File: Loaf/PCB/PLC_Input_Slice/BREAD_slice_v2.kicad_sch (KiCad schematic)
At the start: 12 parts, among them J1 10018783-10200TLF, J2 Conn_01x01_Socket, J3 Conn_01x01_Socket, J4 Conn_01x01_Socket, J5 Conn_01x01_Socket, U2 MCP3208

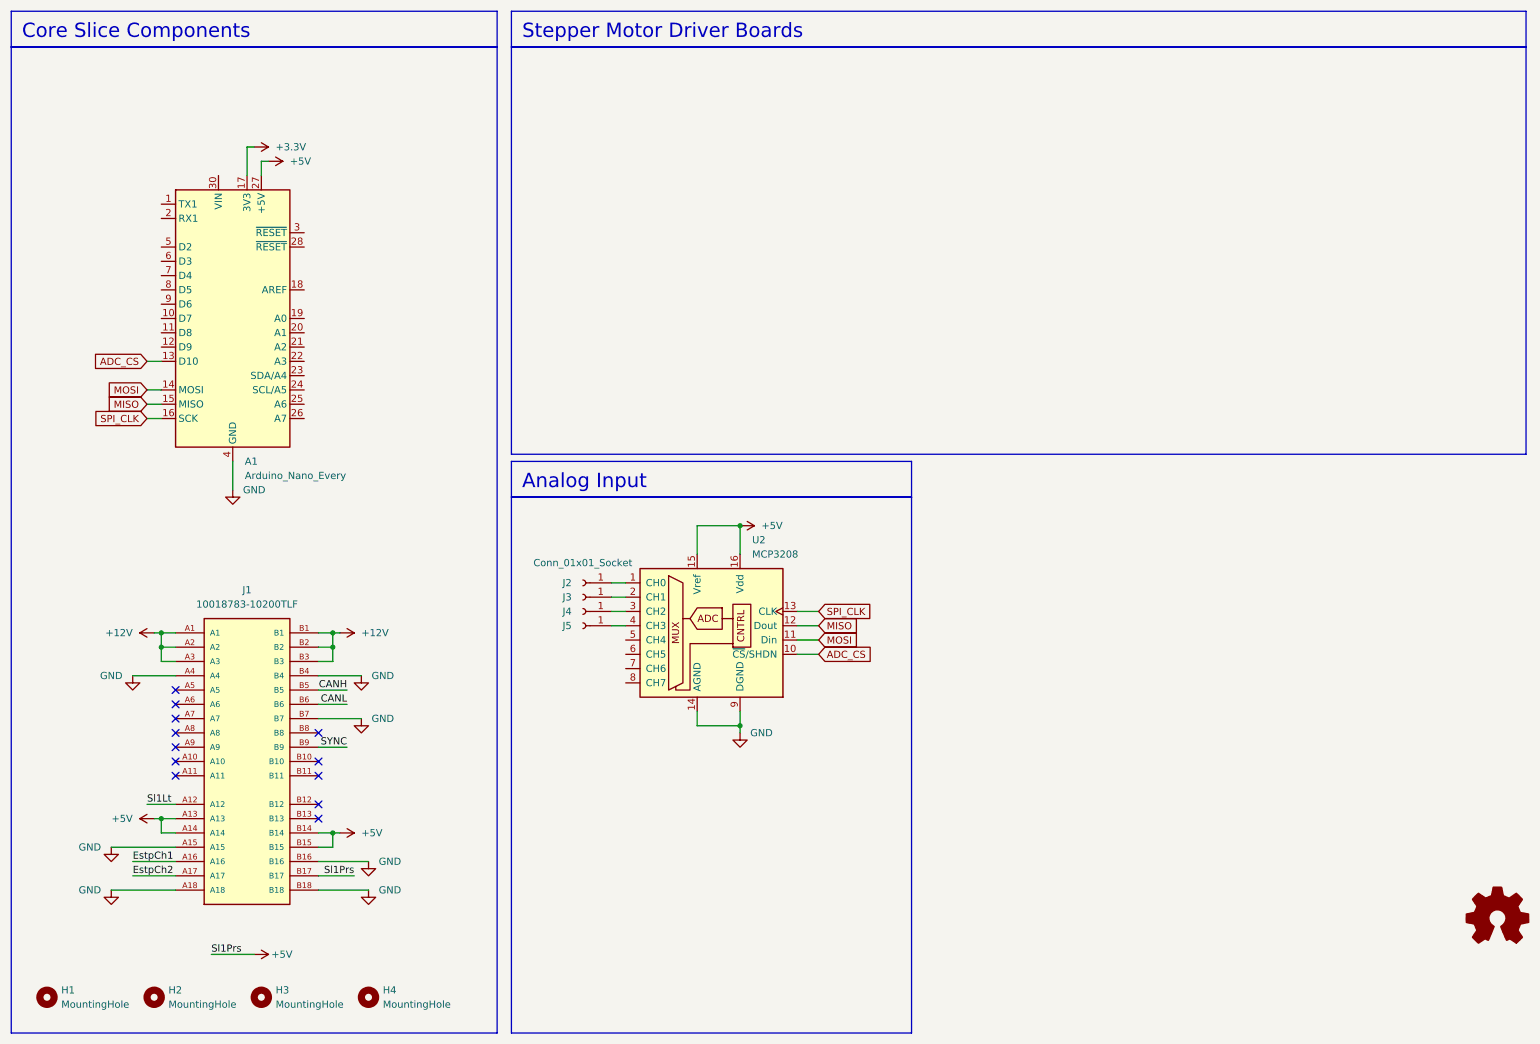
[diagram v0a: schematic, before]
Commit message: Updated IO slice schematic
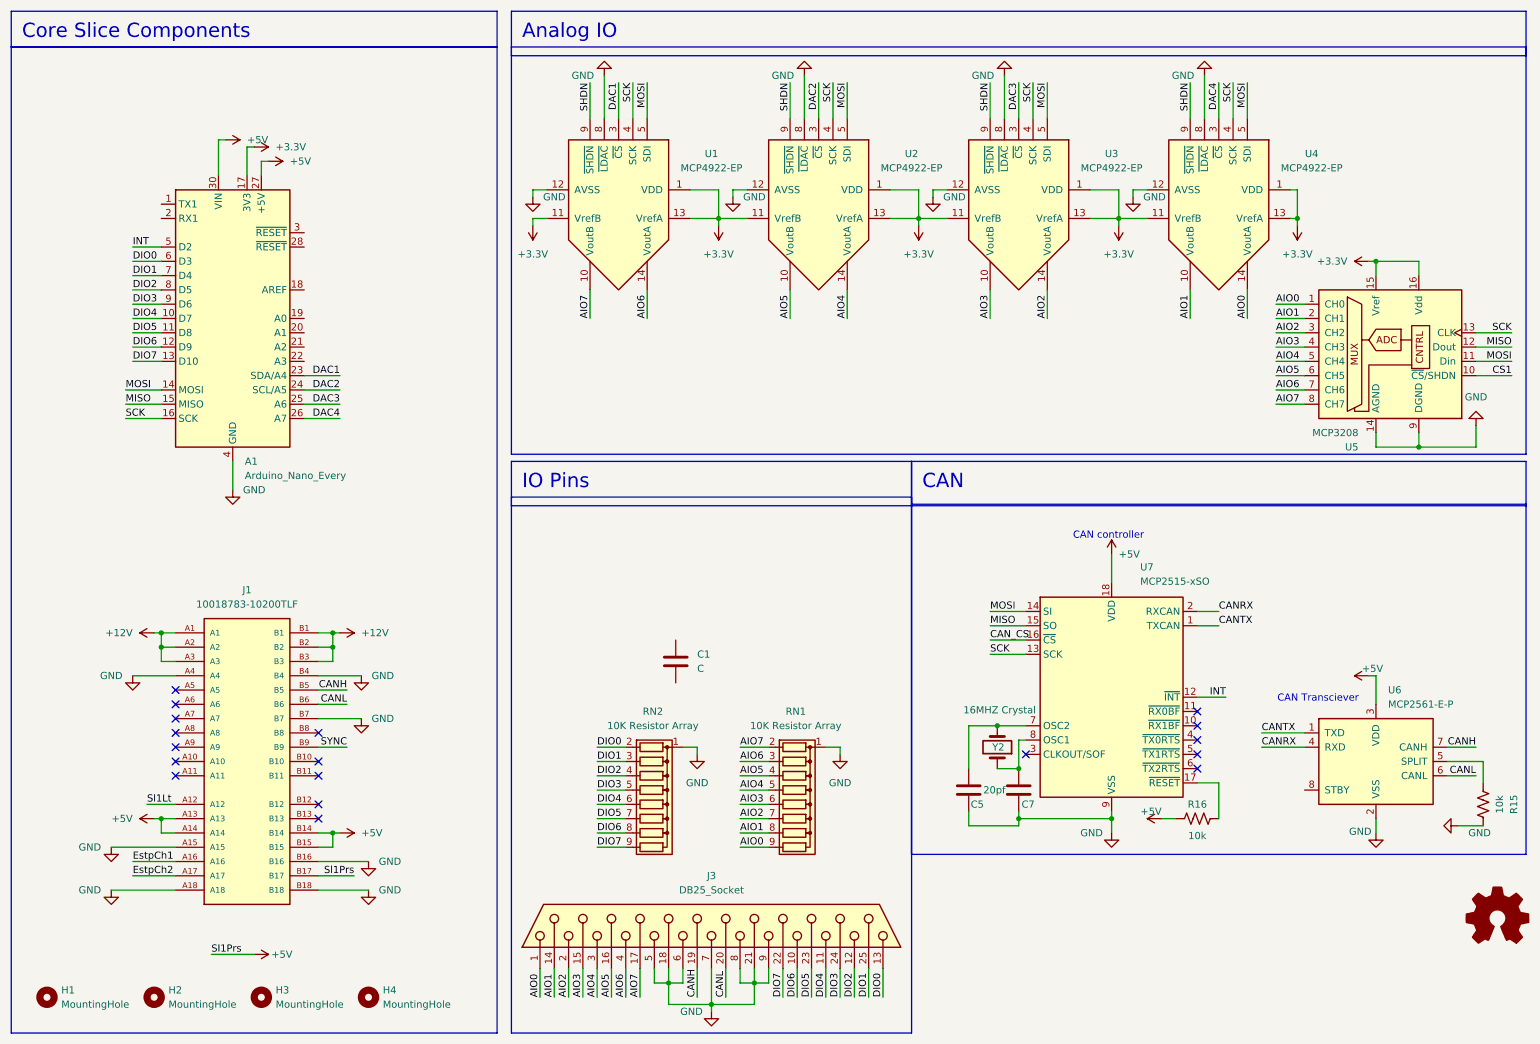
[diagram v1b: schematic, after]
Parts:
- removed J2, J3, J4, J5: Conn_01x01_Socket, Banana_Cliff_FCR7350B_S16N-PC_Horizontal, symbol Connector:Conn_01x01_Socket
- removed U2: MCP3208, DIP-16_W7.62mm_Socket, symbol Analog_ADC:MCP3208
- added C1: C, Package_SO:SOIC-8_3.9x4.9mm_P1.27mm, symbol Device:C
- added C5, C7: 20pf, Capacitor_SMD:C_1206_3216Metric_Pad1.33x1.80mm_HandSolder, symbol Device:C
- added J3: DB25_Socket, DSUB-25_Socket_Horizontal_P2.77x2.84mm_EdgePinOffset4.94mm_Housed_MountingHolesOffset4.94mm, symbol Connector:DB25_Socket
- added R15, R16: 10k, Resistor_SMD:R_1206_3216Metric_Pad1.30x1.75mm_HandSolder, symbol Device:R_US
- added RN1, RN2: 10K Resistor Array, Resistor_THT:R_Array_SIP9, symbol Device:R_Network08
- added U1, U2, U3, U4: MCP4922-EP, Package_DIP:DIP-14_W10.16mm_LongPads, symbol Analog_DAC:MCP4922-EP
- added U5: MCP3208, Package_DIP:DIP-16_W7.62mm_LongPads, symbol Analog_ADC:MCP3208
- added U6: MCP2561-E-P, Package_DIP:DIP-8_W7.62mm, symbol Interface_CAN_LIN:MCP2561-E-P
- added U7: MCP2515-xSO, DIP-18_W7.62mm, symbol Interface_CAN_LIN:MCP2515-xSO
- added Y2: 16MHZ Crystal, LOAF Update:XTAL_ECS-160-20-3X-TR, symbol Device:Crystal
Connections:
- net +3.3V: now also U1.1 (VDD), U1.11 (VrefB), U1.13 (VrefA), U2.1 (VDD), U2.11 (VrefB), U2.13 (VrefA), U3.1 (VDD), U3.11 (VrefB), U3.13 (VrefA), U4.1 (VDD), U4.11 (VrefB), U4.13 (VrefA), U5.15 (Vref), U5.16 (Vdd)
- net +5V: now also A1.30 (VIN), R16.2, U6.3 (VDD), U7.18 (VDD)
- net CANH: now also J3.19 (P19), U6.7 (CANH)
- net CANL: now also J3.20 (P20), U6.6 (CANL)
- net GND: now also C5.2, C7.2, J3.18 (P18), J3.21 (P21), J3.5, J3.6, J3.7, J3.8, J3.9, R15.1, RN1.1 (common), RN2.1 (common), U1.12 (AVSS), U1.8 (~{LDAC}), U2.12 (AVSS), U2.8 (~{LDAC}), U3.12 (AVSS), U3.8 (~{LDAC}), U4.12 (AVSS), U4.8 (~{LDAC}), U5.14 (AGND), U5.9 (DGND), U6.2 (VSS), U7.9 (VSS)
- net MISO: now also U5.12 (Dout), U7.15 (SO)
- net MOSI: now also U1.5 (SDI), U2.5 (SDI), U3.5 (SDI), U4.5 (SDI), U5.11 (Din), U7.14 (SI)
- net DIO4: now reaches A1.10 (D7)
- net DIO4: now also J3.11, RN2.6 (R5)
- net DIO5: now reaches A1.11 (D8)
- net DIO5: now also J3.23 (P23), RN2.7 (R6)
- net DIO6: now reaches A1.12 (D9)
- net DIO6: now also J3.10, RN2.8 (R7)
- net DAC1: now reaches A1.23 (SDA/A4)
- net DAC1: now also U1.3 (~{CS})
- net DAC2: now reaches A1.24 (SCL/A5)
- net DAC2: now also U2.3 (~{CS})
- net DAC3: now reaches A1.25 (A6)
- net DAC3: now also U3.3 (~{CS})
- net DAC4: now reaches A1.26 (A7)
- net DAC4: now also U4.3 (~{CS})
- net INT: now reaches A1.5 (D2)
- net INT: now also U7.12 (~{INT})
- net DIO0: now reaches A1.6 (D3)
- net DIO0: now also J3.13, RN2.2 (R1)
- net DIO1: now reaches A1.7 (D4)
- net DIO1: now also J3.25 (P25), RN2.3 (R2)
- net DIO2: now reaches A1.8 (D5)
- net DIO2: now also J3.12, RN2.4 (R3)
- net DIO3: now reaches A1.9 (D6)
- net DIO3: now also J3.24 (P24), RN2.5 (R4)
- net ADC_CS renamed DIO7
- net DIO7: now also J3.22 (P22), RN2.9 (R8)
- net SPI_CLK renamed SCK
- net SCK: now also U1.4 (SCK), U2.4 (SCK), U3.4 (SCK), U4.4 (SCK), U5.13 (CLK), U7.13 (SCK)
- new net: C5.1, U7.7 (OSC2), Y2.2
- new net: R15.2, U6.5 (SPLIT)
- new net: C7.1, U7.8 (OSC1), Y2.1
- new net: R16.1, U7.17 (~{RESET})
- new net AIO0: J3.1, RN1.9 (R8), U4.14 (VoutA), U5.1 (CH0)
- new net AIO1: J3.14 (P14), RN1.8 (R7), U4.10 (VoutB), U5.2 (CH1)
- new net AIO2: J3.2, RN1.7 (R6), U3.14 (VoutA), U5.3 (CH2)
- new net AIO3: J3.15 (P15), RN1.6 (R5), U3.10 (VoutB), U5.4 (CH3)
- new net AIO4: J3.3, RN1.5 (R4), U2.14 (VoutA), U5.5 (CH4)
- new net AIO5: J3.16 (P16), RN1.4 (R3), U2.10 (VoutB), U5.6 (CH5)
- new net AIO6: J3.4, RN1.3 (R2), U1.14 (VoutA), U5.7 (CH6)
- new net AIO7: J3.17 (P17), RN1.2 (R1), U1.10 (VoutB), U5.8 (CH7)
- new net CANRX: U6.4 (RXD), U7.2 (RXCAN)
- new net CANTX: U6.1 (TXD), U7.1 (TXCAN)
- new net CAN_CS: U7.16 (~{CS})
- new net CS1: U5.10 (~{CS}/SHDN)
- new net SHDN: U1.9 (~{SHDN}), U2.9 (~{SHDN}), U3.9 (~{SHDN}), U4.9 (~{SHDN})
- no-connect marks 12 -> 18
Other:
- note added: "CAN Transciever"
- note added: "CAN controller"
